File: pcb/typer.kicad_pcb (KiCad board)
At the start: 2 copper layers, 182.8 x 158.9 mm, 47 parts, among them J2 3.5mm, SW0:0 SW0:0, SW0:1 SW0:1, SW0:2 SW0:2, SW0:3 SW0:3, SW0:4 SW0:4, SW1:0 SW1:0, SW1:1 SW1:1, SW1:2 SW1:2, SW1:3 SW1:3, SW1:4 SW1:4, SW2:0 SW2:0, SW2:1 SW2:1, SW2:2 SW2:2, SW2:3 SW2:3, SW2:4 SW2:4, SW3:0 SW3:0, SW3:1 SW3:1, SW3:2 SW3:2, SW3:3 SW3:3, SW3:4 SW3:4, SW4:0 SW4:0, SW4:1 SW4:1, SW4:2 SW4:2, SW4:3 SW4:3, SW4:4 SW4:4, SW5:0 SW5:0, SW5:1 SW5:1, SW5:2 SW5:2, SW5:3 SW5:3, SW5:4 SW5:4, SW6:0 SW6:0, SW6:1 SW6:1, SW6:2 SW6:2, SW6:3 SW6:3, SW6:4 SW6:4, SW7:2 SW7:2, SW7:3 SW7:3, SW7:4 SW7:4, U1 rp2040-zero

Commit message: column traces
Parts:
- moved U1 1.56 mm to (137.9, 42.6)
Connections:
- J2 pad 2: unconnected-(J2-Pad2) -> GND
- J2 pad 3: unconnected-(J2-Pad3) -> 5V
- J2 pad 4: unconnected-(J2-Pad4) -> RX
- J2 pad 5: unconnected-(J2-Pad5) -> TX
- U1 pad 1: unconnected-(U1-0-Pad1) -> TX
- U1 pad 10: unconnected-(U1-9-Pad10) -> COLUMN7
- U1 pad 15: unconnected-(U1-14-Pad15) -> ROW0
- U1 pad 16: unconnected-(U1-15-Pad16) -> ROW1
- U1 pad 17: unconnected-(U1-26-Pad17) -> ROW2
- U1 pad 18: unconnected-(U1-27-Pad18) -> ROW3
- U1 pad 19: unconnected-(U1-28-Pad19) -> ROW4
- U1 pad 2: unconnected-(U1-1-Pad2) -> RX
- U1 pad 22: unconnected-(U1-GND-Pad22) -> GND
- U1 pad 23: unconnected-(U1-5V-Pad23) -> 5V
- U1 pad 3: unconnected-(U1-2-Pad3) -> COLUMN0
- U1 pad 4: unconnected-(U1-3-Pad4) -> COLUMN1
- U1 pad 5: unconnected-(U1-4-Pad5) -> COLUMN2
- U1 pad 6: unconnected-(U1-5-Pad6) -> COLUMN3
- U1 pad 7: unconnected-(U1-6-Pad7) -> COLUMN4
- U1 pad 8: unconnected-(U1-7-Pad8) -> COLUMN5
- U1 pad 9: unconnected-(U1-8-Pad9) -> COLUMN6
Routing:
- net COLUMN6: track 0.00 -> 210.2 mm
- net COLUMN2: track 0.00 -> 184.7 mm
- net COLUMN5: track 0.00 -> 180.8 mm
- net COLUMN1: track 0.00 -> 179.7 mm
- net COLUMN0: track 112.6 -> 290.8 mm
- net COLUMN3: track 0.00 -> 151.4 mm
- net COLUMN7: track 18.4 -> 161.3 mm
- net COLUMN4: track 0.00 -> 125.4 mm
- net ROW4: track 188.8 -> 213.7 mm
- net ROW3: track 235.9 -> 256.7 mm
- net Net-(SW5:4-A): track 40.9 -> 59.5 mm, vias 0 -> 1
- net ROW2: track 234.2 -> 252.1 mm
- net Net-(SW6:4-A): track 40.9 -> 58.5 mm
- net ROW1: track 193.5 -> 206.2 mm
- net ROW0: track 195.3 -> 205.5 mm
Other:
- outline, holes or cut-outs redrawn

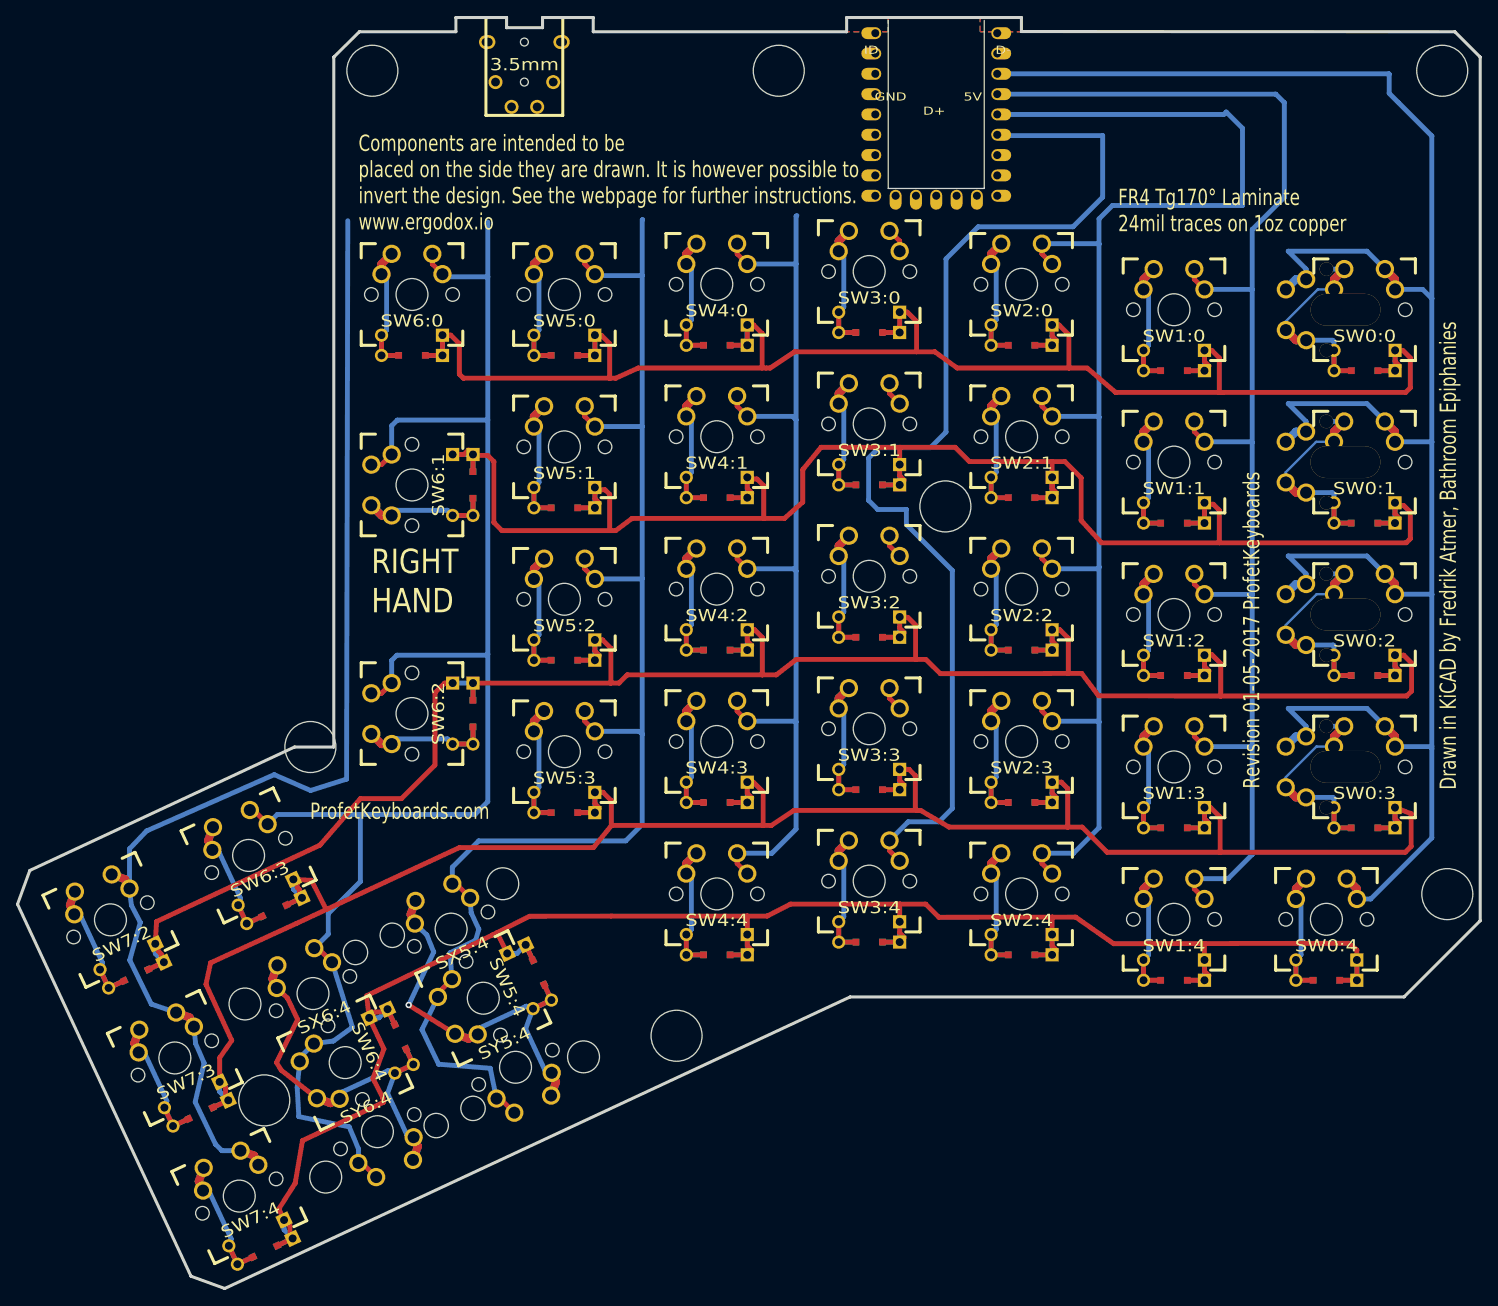
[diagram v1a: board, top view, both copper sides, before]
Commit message: lib changes removed col tacres
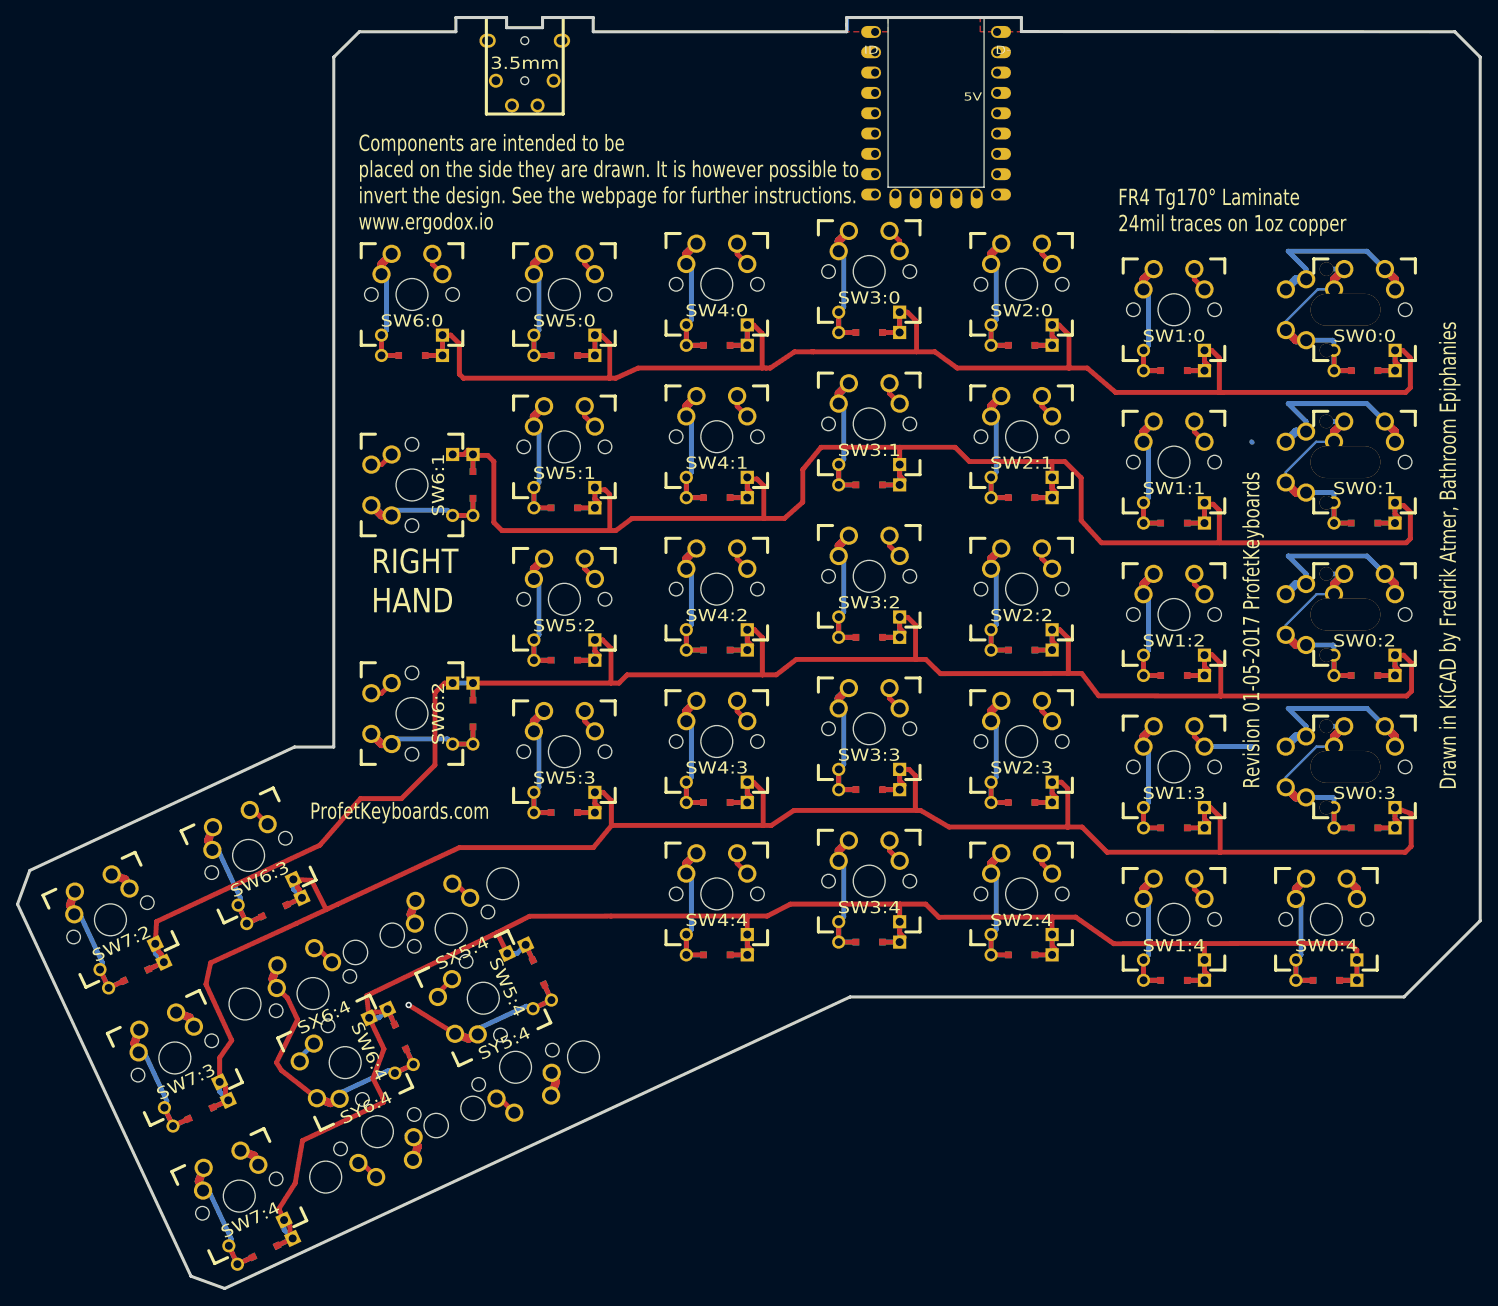
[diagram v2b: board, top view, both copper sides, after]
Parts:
- removed H99: MECHANICAL, Library:ErgoDOXmech
- moved J2 0.18 mm to (86.5, 30.5)
- moved U1 0.15 mm to (137.9, 42.4)
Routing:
- net COLUMN6: track 210.2 -> 21.5 mm
- net COLUMN0: track 290.8 -> 112.6 mm
- net COLUMN2: track 184.7 -> 15.3 mm
- net COLUMN5: track 180.8 -> 21.4 mm
- net COLUMN1: track 179.7 -> 21.5 mm
- net COLUMN7: track 161.3 -> 18.4 mm
- net COLUMN3: track 151.4 -> 15.5 mm
- net COLUMN4: track 125.4 -> 15.3 mm
- net Net-(SW5:4-A): track 59.5 -> 39.4 mm
- net Net-(SW6:4-A): track 58.5 -> 50.1 mm
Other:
- outline, holes or cut-outs redrawn
- board text removed: "D+"
- board text removed: "GND"

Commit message: row connected
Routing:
- net ROW4: track 213.7 -> 356.8 mm, vias 0 -> 8
- net ROW3: track 256.7 -> 349.4 mm, vias 0 -> 6
- net ROW2: track 252.1 -> 323.2 mm, vias 0 -> 4
- net ROW1: track 206.2 -> 249.6 mm, vias 0 -> 2
- net ROW0: track 205.7 -> 231.5 mm

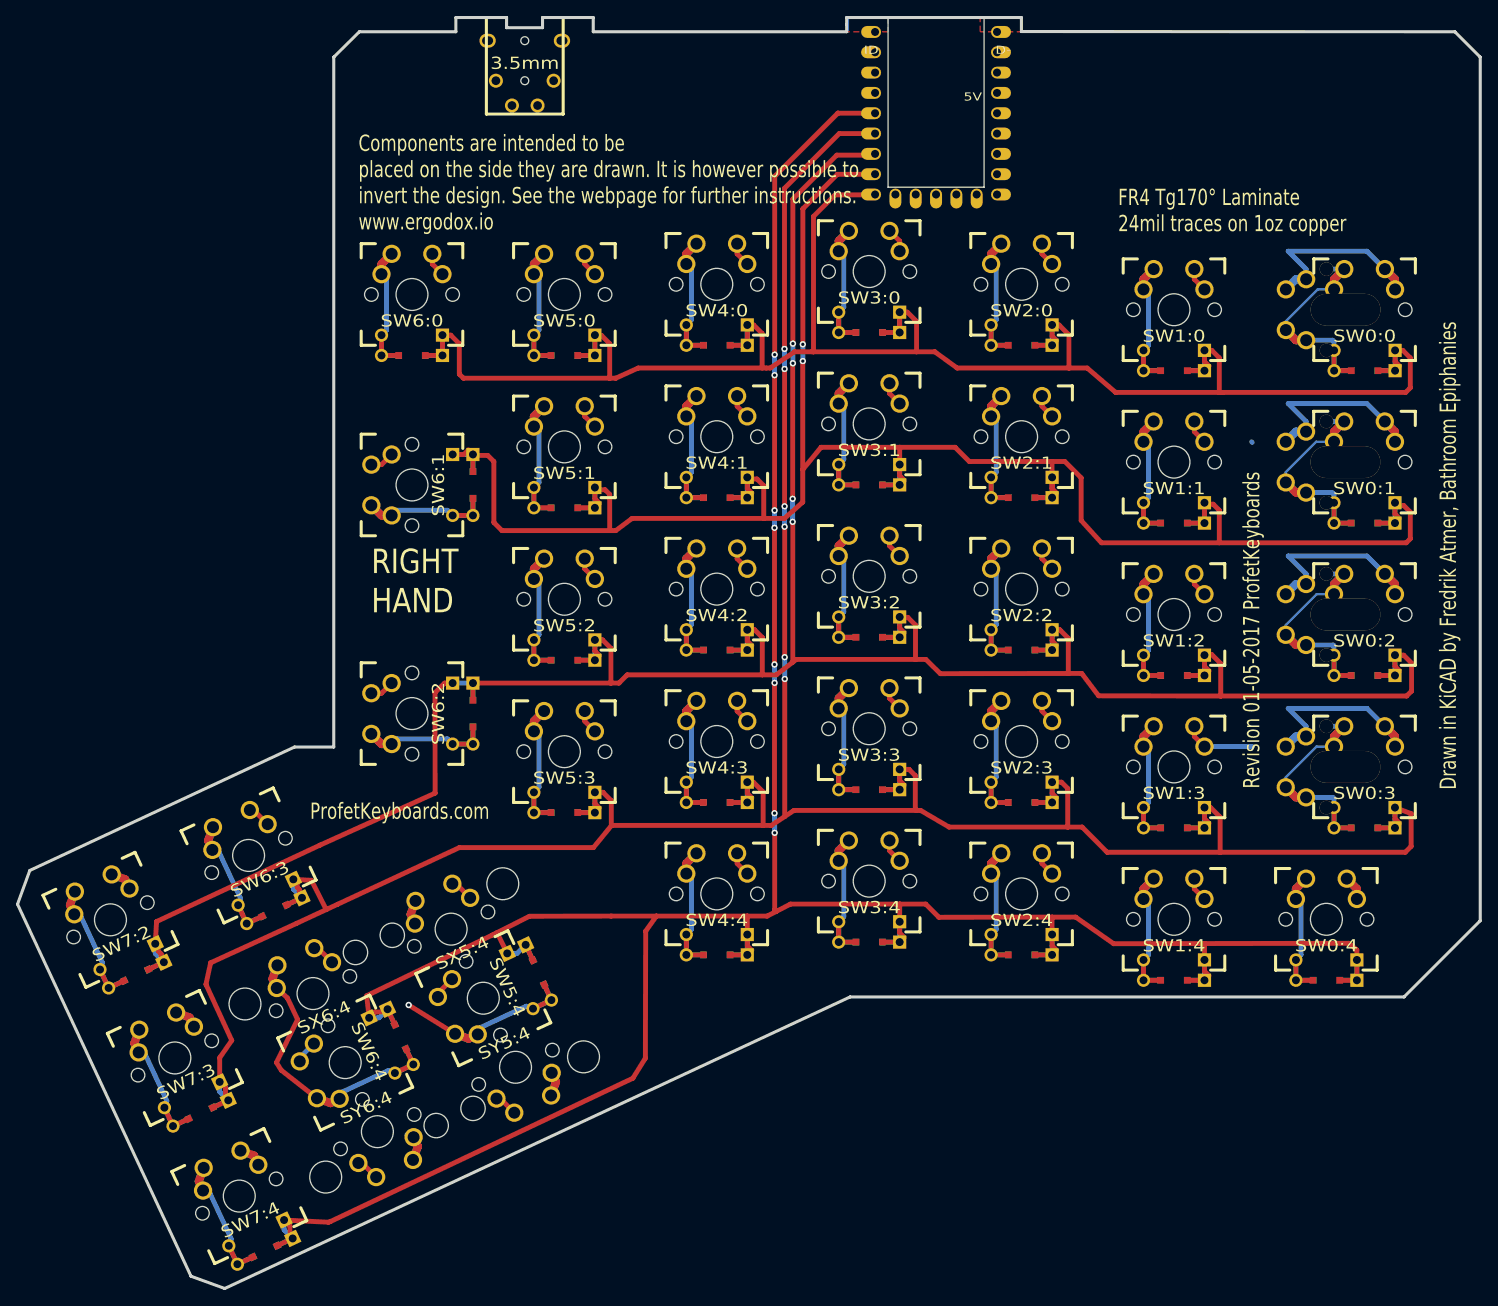
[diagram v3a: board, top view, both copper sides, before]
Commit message: traces added
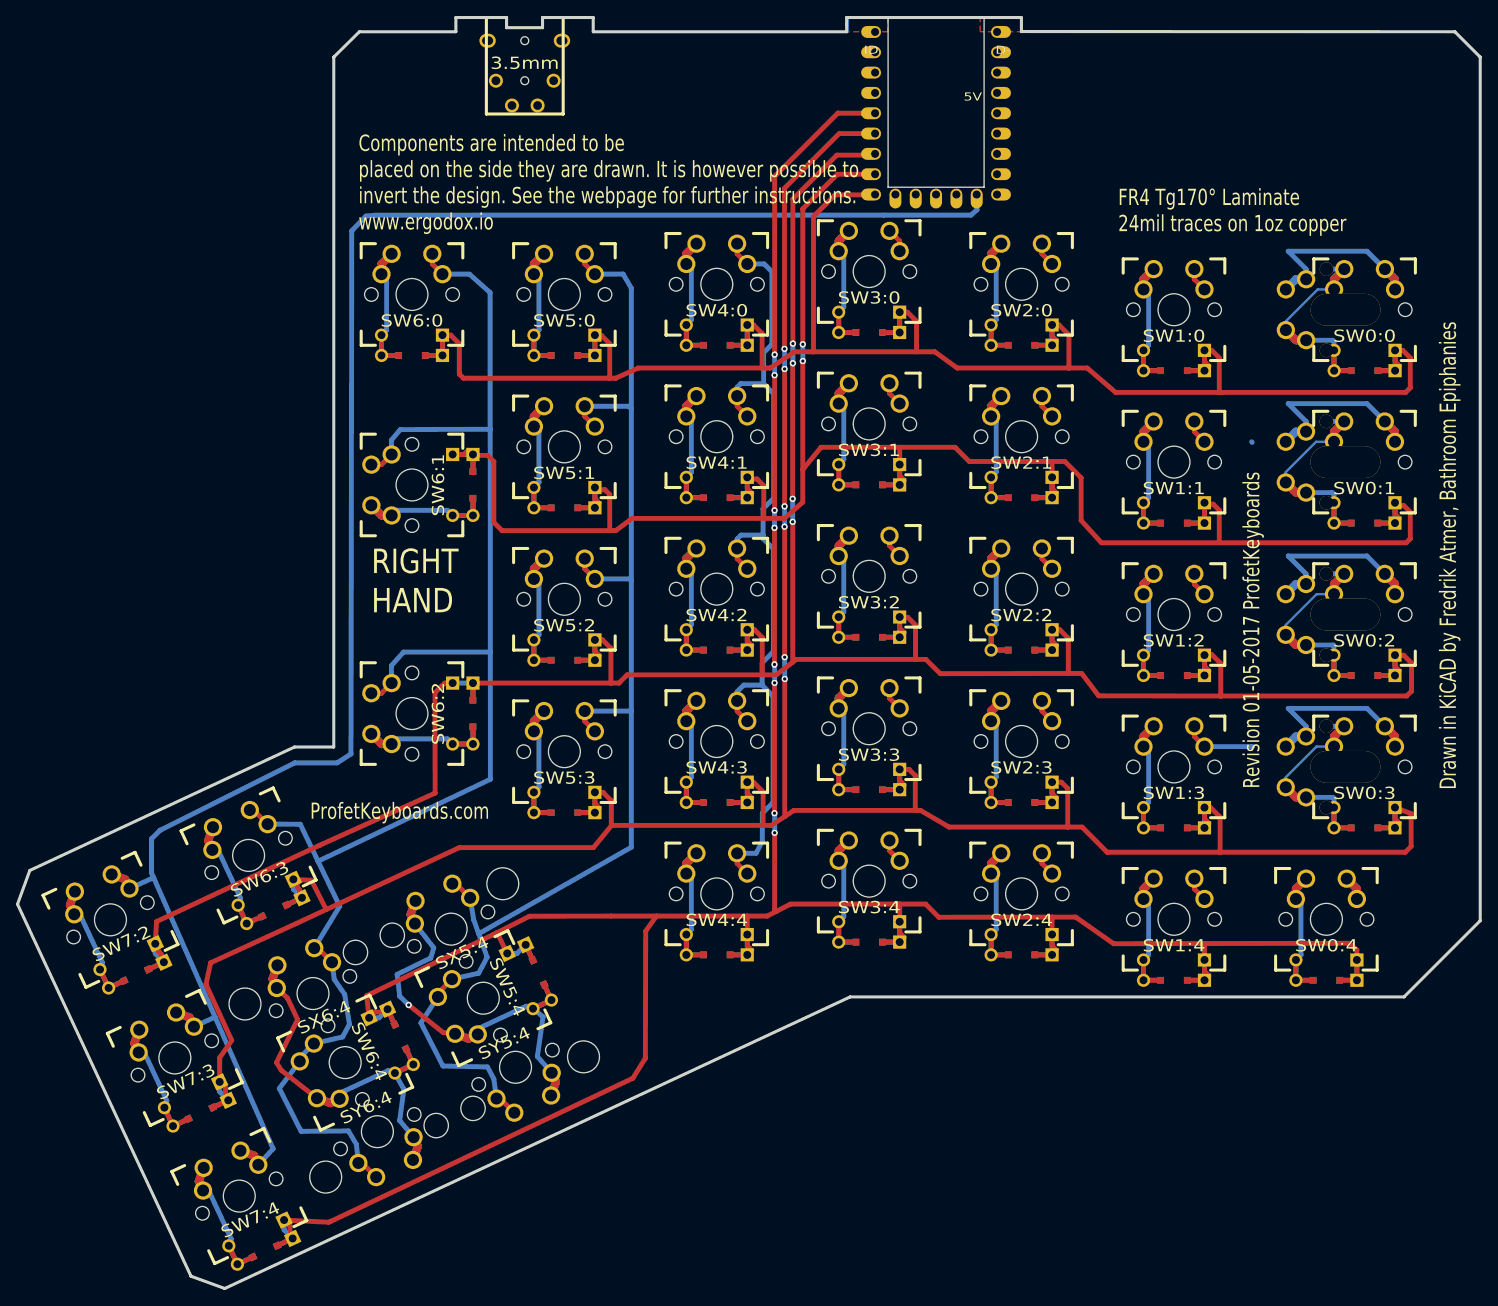
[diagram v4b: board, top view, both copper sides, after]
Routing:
- net COLUMN7: track 18.4 -> 243.5 mm
- net COLUMN6: track 21.5 -> 198.8 mm
- net COLUMN5: track 21.4 -> 168.3 mm
- net COLUMN4: track 15.3 -> 111.7 mm
- net Net-(SW5:4-A): track 39.4 -> 63.1 mm
- net Net-(SW6:4-A): track 50.1 -> 59.1 mm
